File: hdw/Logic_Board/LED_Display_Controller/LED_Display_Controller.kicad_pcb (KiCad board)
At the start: 4 copper layers, 855 parts, among them J1101 USB_B_Mini, J1401 Encoder Ext, J1601 POS5P EXT, J1602 POS5P PGOOD, J1603 POS5P_THWN, J1604 POS5P_RUN, J201 +12V IN, J202 GND IN, J203 +12V IN AUX, J204 Master Power SW, J2901 STRING 1, J2902 STRING 2, J2903 STRING 3, J2904 STRING 4, J3001 USB UART, J3002 WIFI UART, J3003 FLASH SPI, J3004 Panel TP, J501 PICKIT3, J901 ESP8266 Socket, Q201 IPC100N04S51R7ATMA1, Q202 IPC100N04S51R7ATMA1, Q501 BSS214NW, Q901 BSS214NW, SW1401 Display Enable, SW1402 Brightness/Enable, SW501 MRST, U1001 ISO7321C, U1101 LT6700-1-S6, U1102 FT234XD, U1103 74LVC1G06, U1104 TPD3S014DBVR, U1201 74LVC1G06, U1202 74LVC1G06, U1203 74LVC1G06, U1204 74LVC1G06, U1205 74LVC1G06, U1206 74LVC1G06, U1207 74LVC1G06, U1301 74LVC1G06, U1302 74LVC1G06, U1303 74LVC1G06, U1304 74LVC1G06, U1401 MAX6816, U1402 74LVC2G14, U1403 74LVC1G79, U1601 LM1117-ADJ, U1602 NUP2202, U1603 74LVC1G17, U1604 74LVC1G17, U1605 74LVC1G17, U1606 NUP2202, U1701 CY7C1010DV33, U1801 SST25PF020B, U1901 SST25PF020B, U2001 SST25PF020B, U201 LTC4365DDB, U2101 SST25PF020B, U2201 SST25PF020B, U2301 SST25PF020B, U2401 SST25PF020B, U2501 SST25PF020B, U2601 74HCT541, U2602 74HCT541, U2701 74HCT541, U2702 74HCT541, U2801 74LVC1G32, U2802 74HCT541, U301 LTC3605A_UF, U401 LTC3624DD, U601 PIC32MZ2048EFH144_IPL

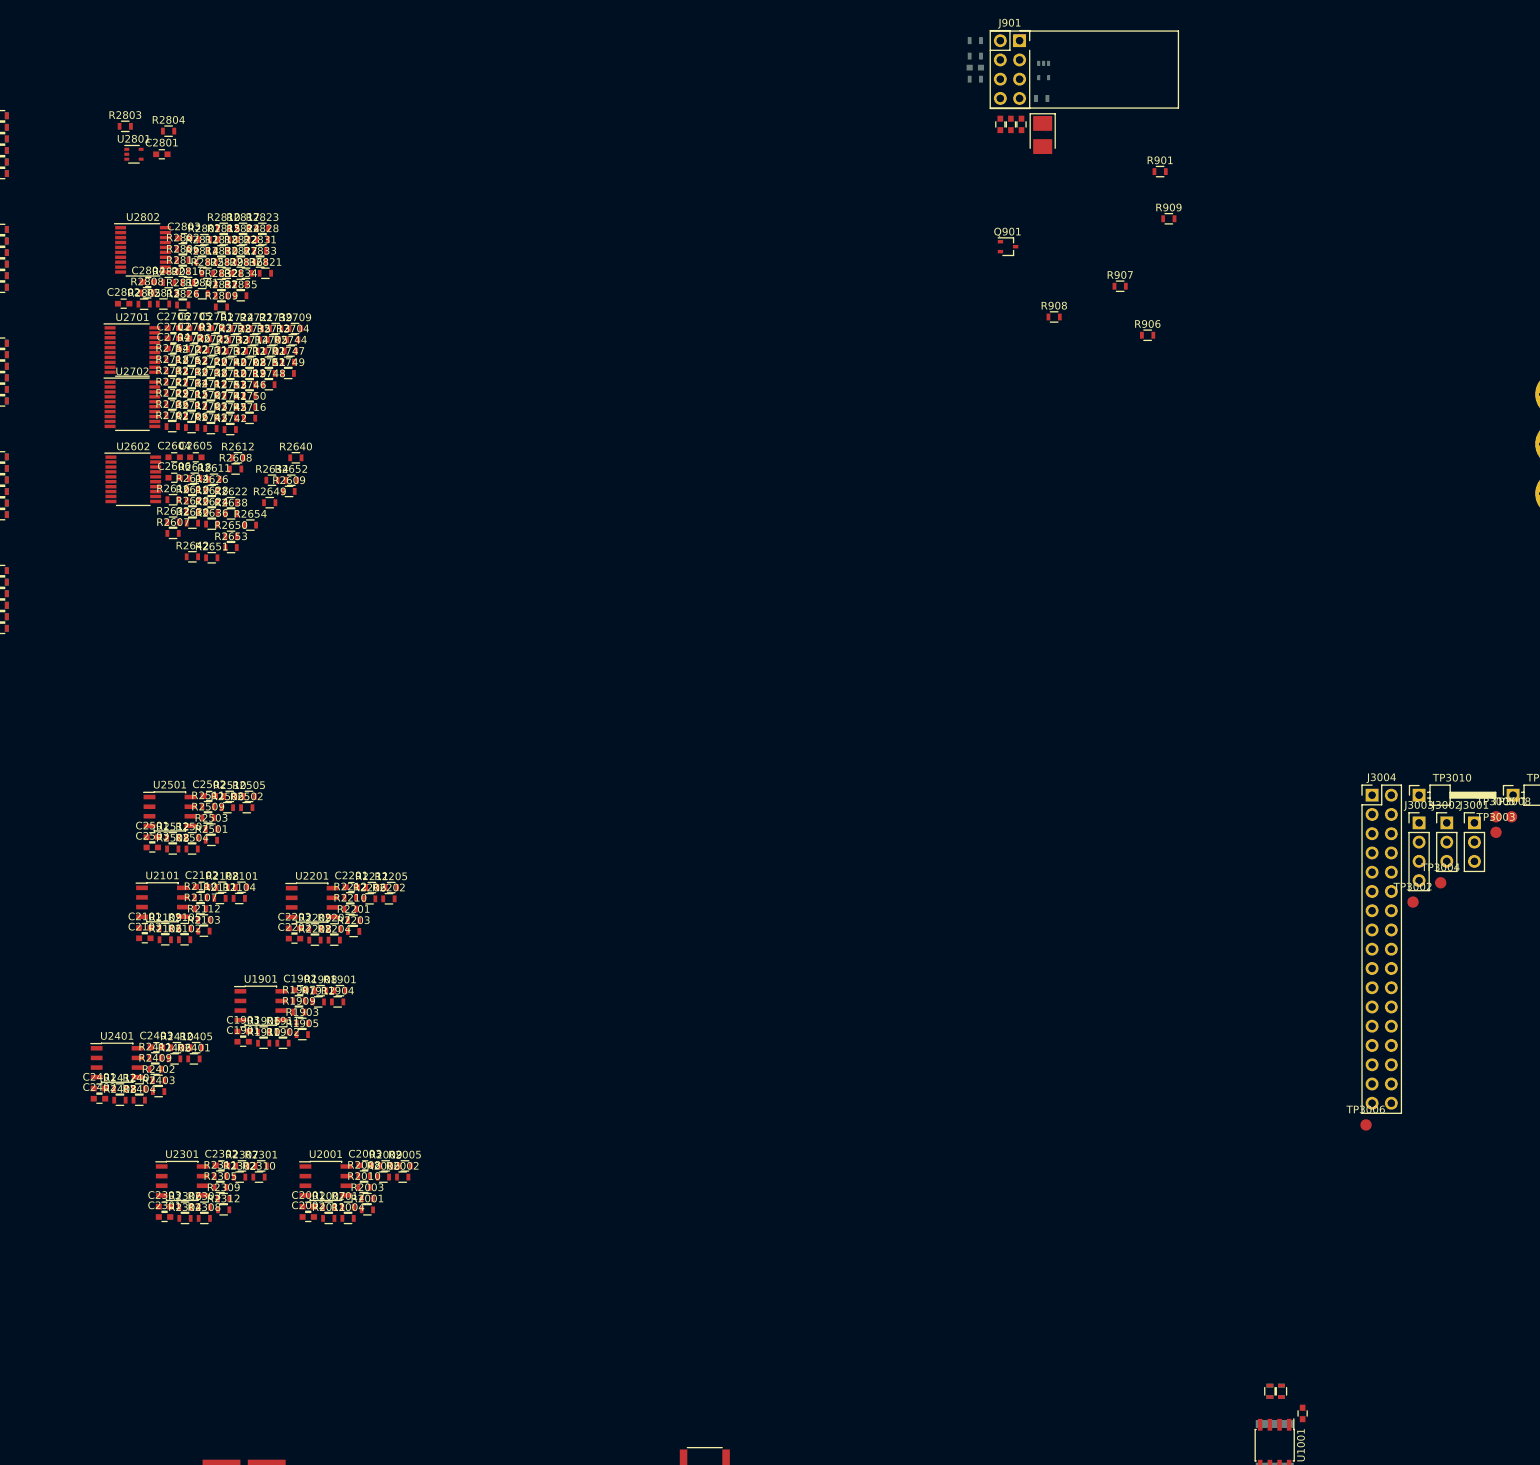
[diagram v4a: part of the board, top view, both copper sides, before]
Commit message: Placed parts for WIFI module
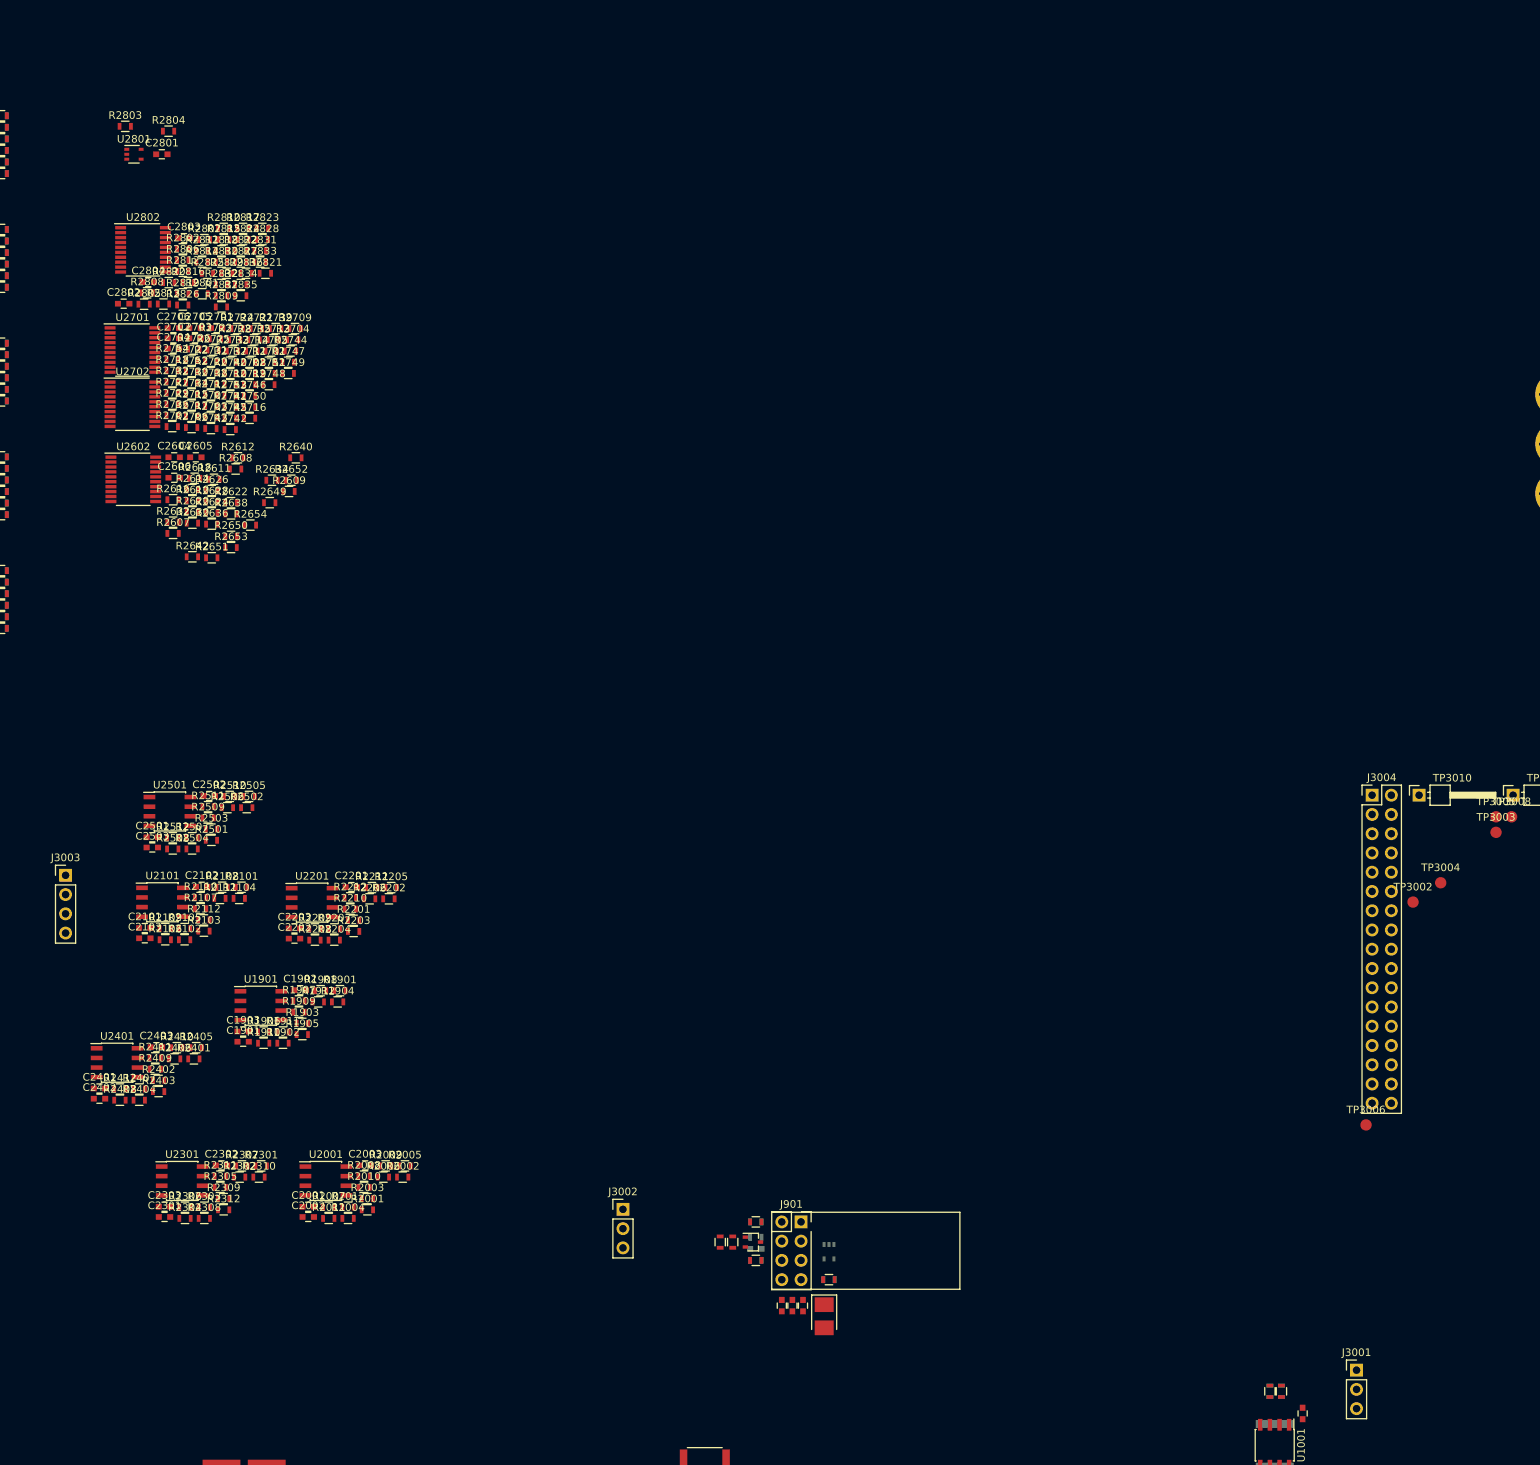
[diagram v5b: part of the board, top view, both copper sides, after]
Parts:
- moved J3003 178.7 mm to (144.8, 134.6)
- moved R903 158.5 mm to (235.8, 180.3)
- moved R904 158.5 mm to (235.8, 182.4)
- moved C905 158.5 mm to (235.8, 183.9)
- moved R905 158.5 mm to (235.8, 185.4)
- moved C903 158.5 mm to (240.7, 191.4)
- moved C901 158.5 mm to (244.9, 192.8)
- moved C902 158.5 mm to (242.1, 191.4)
- moved C904 158.5 mm to (239.3, 191.4)
- moved J901 158.5 mm to (241.8, 180.3)
- moved D901 158.4 mm to (245.5, 184.3)
- moved R902 158.3 mm to (245.5, 188.0)
- moved R901 152.6 mm to (245.5, 188.0), turned to 180 degrees
- moved R909 143.1 mm to (235.8, 180.3)
- moved R907 136.1 mm to (232.8, 183.0), turned to 90 degrees
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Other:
- board text added: "WIFI"
